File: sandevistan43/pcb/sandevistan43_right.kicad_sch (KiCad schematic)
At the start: 48 parts, among them J2 TRRS, SW23 SW_PUSH, SW24 SW_PUSH, SW25 SW_PUSH, SW26 SW_PUSH, SW27 SW_PUSH, SW28 SW_PUSH, SW29 SW_PUSH, SW30 SW_PUSH, SW31 SW_PUSH, SW32 SW_PUSH, SW33 SW_PUSH, SW34 SW_PUSH, SW35 SW_PUSH, SW36 SW_PUSH, SW37 SW_PUSH, SW38 SW_PUSH, SW39 SW_PUSH, SW40 SW_PUSH, SW41 SW_PUSH, SW42 SW_PUSH, SW43 SW_PUSH, U2 Pico

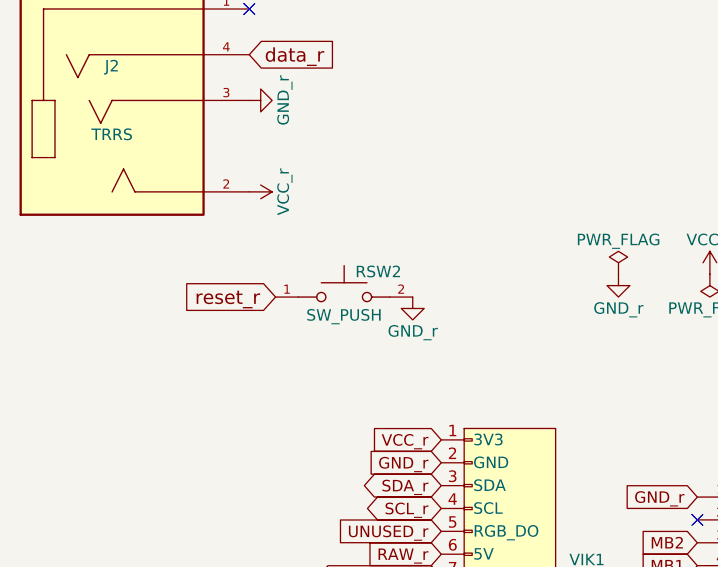
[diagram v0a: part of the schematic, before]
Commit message: Make footprints/symbols common and use easier to solder reset button
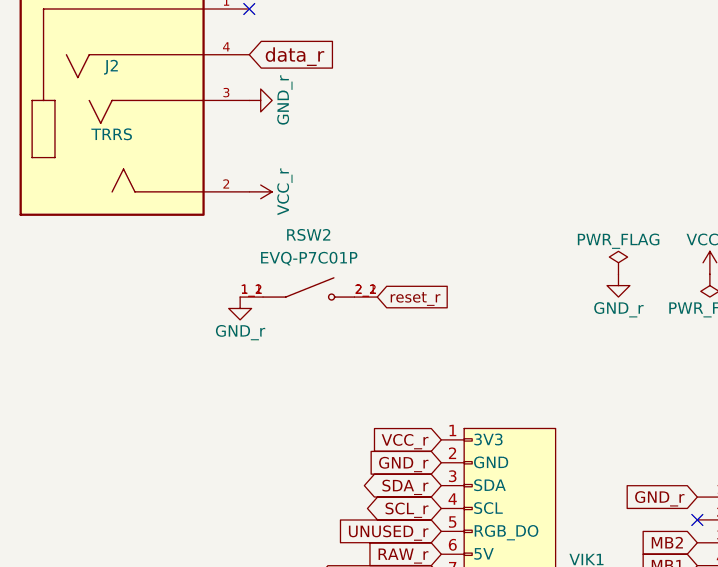
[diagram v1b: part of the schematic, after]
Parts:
- removed RSW2: SW_PUSH, TL6340AF160Q:SW_TL6340AF160Q, symbol TL6340AF160Q:TL6340AF160Q
- added RSW2: EVQ-P7C01P, EVQ-P7C01P:SW_EVQ-P7C01P, symbol EVQ-P7C01P:EVQ-P7C01P
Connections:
- net GND_r: now also RSW2.1_1, RSW2.1_2
- net reset_r: now also RSW2.2_1, RSW2.2_2
